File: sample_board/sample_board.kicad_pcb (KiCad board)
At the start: 2 copper layers, 102 x 40 mm, 50 parts, among them J1 Conn_01x10, J2 Conn_01x10, J3 ICSP, J4 USB_B_Micro, U1 ATmega32U4-A, Y1 16MHz

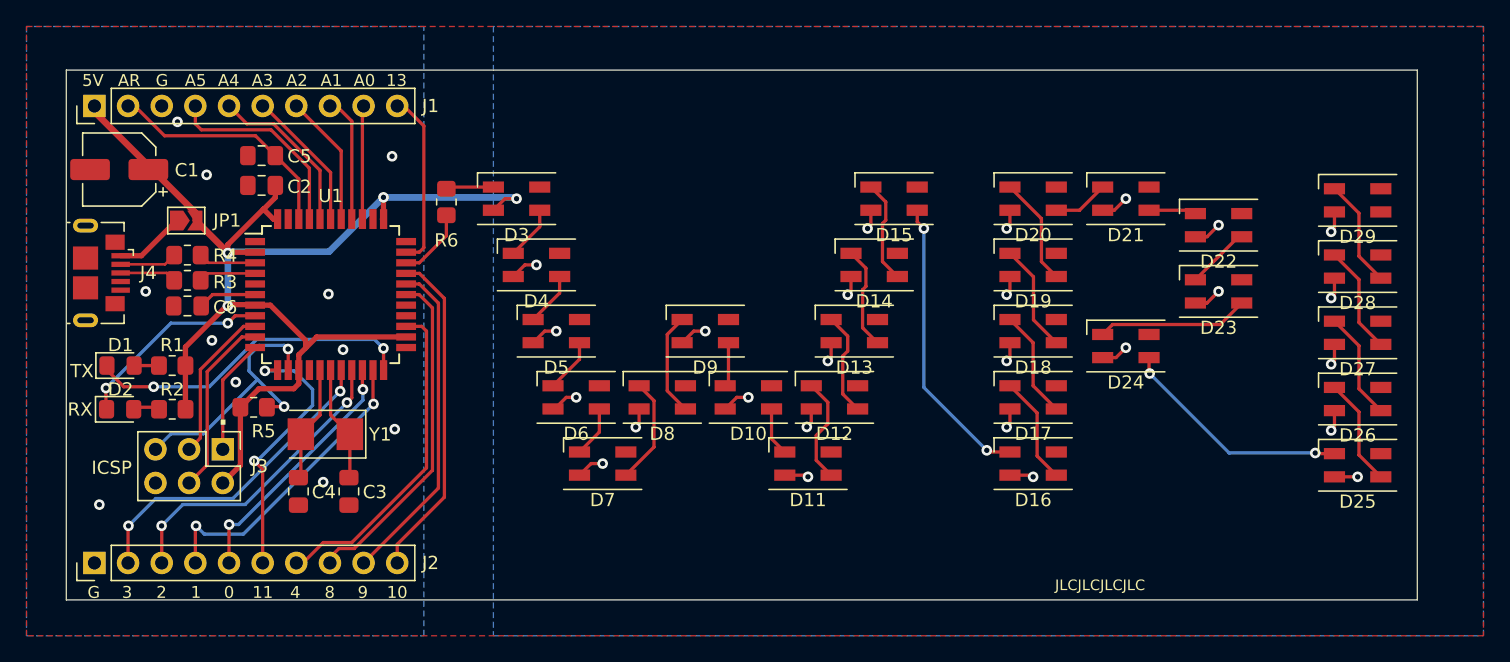
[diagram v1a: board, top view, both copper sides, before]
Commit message: sample board rev2; added button
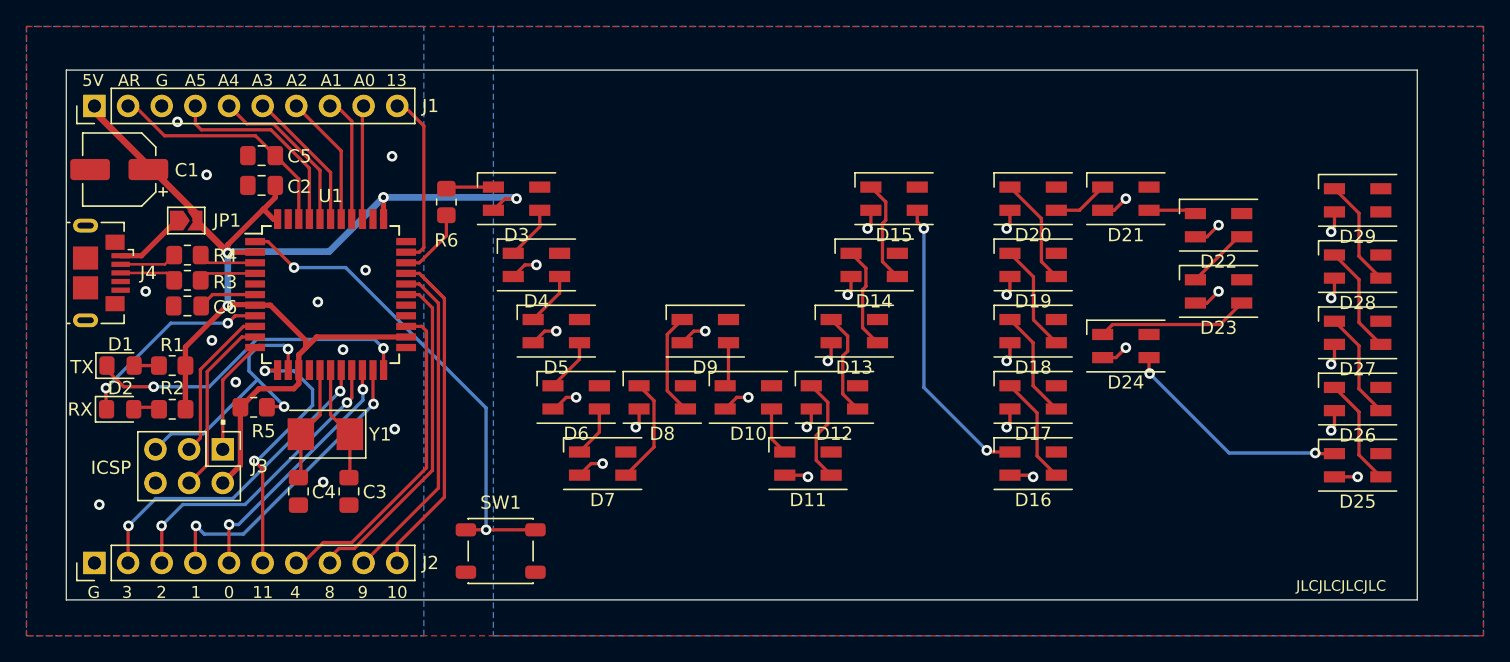
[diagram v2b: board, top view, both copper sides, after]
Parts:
- removed the G*** at (126.0, 162.0)
- added SW1: SW_Push, Button_Switch_SMD:SW_SPST_PTS647_Sx38, F.Cu at (80.8, 161.6)
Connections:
- U1 pad 1: unconnected-(U1-PE6-Pad1) -> /BUTTON
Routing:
- net /BUTTON: track 0.00 -> 37.1 mm, vias 0 -> 2
- net /D10: track 25.6 -> 28.0 mm
- net GND: vias 11 -> 12
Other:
- board text added: "github.com/ieee-wpi"
- board text added: "rev2 | 10.06.24"
- board text removed: "github.com/dgorbunov"
- board text removed: "rev1 | 04.10.24"
